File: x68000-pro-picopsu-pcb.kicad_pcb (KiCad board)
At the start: 2 copper layers, 209 x 98 mm, 27 parts, among them J1 Fan Header, J2 Screw_Terminal_01x07, J3 Screw_Terminal_01x07, J4 PicoPSU, U1 74LS04

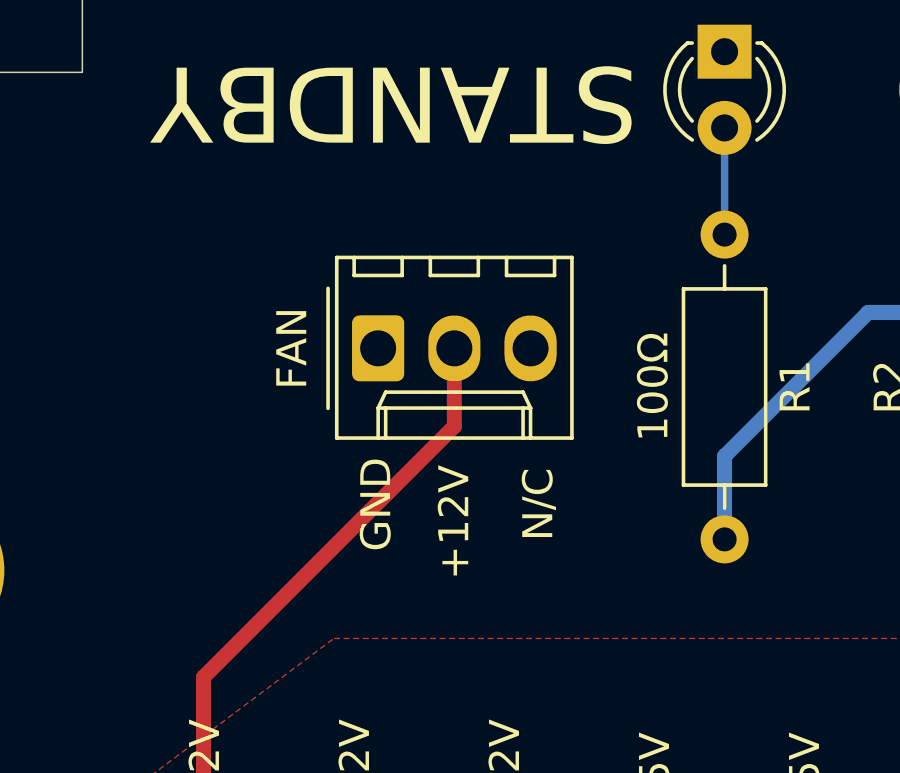
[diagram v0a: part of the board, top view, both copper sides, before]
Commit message: Move fan hed up a bit to make more room for wires
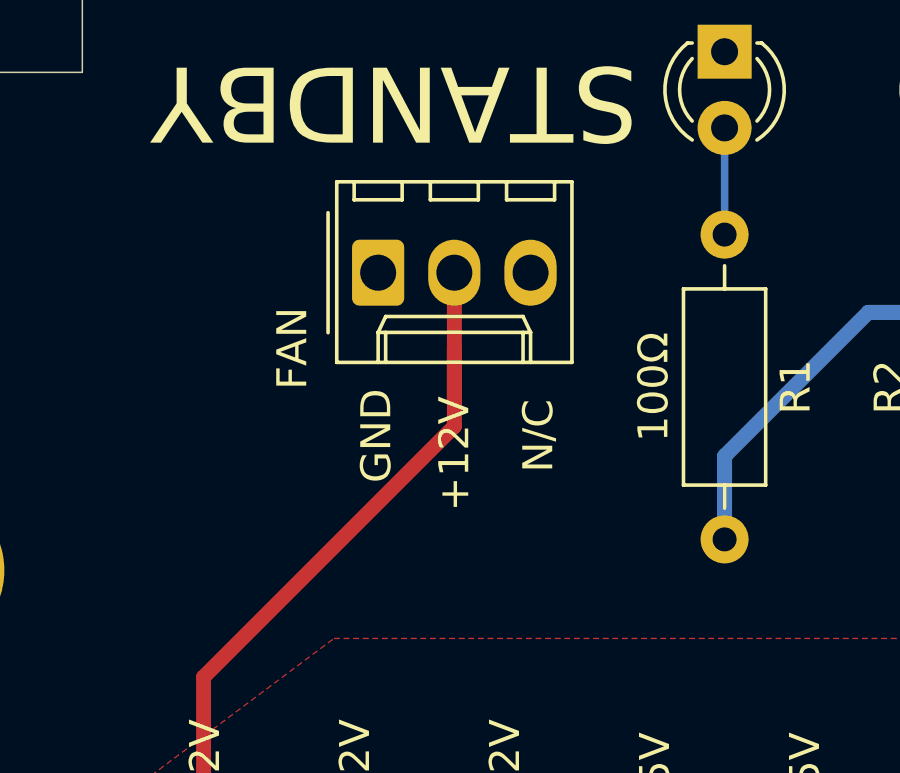
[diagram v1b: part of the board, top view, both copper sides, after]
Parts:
- moved J1 2.52 mm to (41.9, 90.7)
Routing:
- net /PSU_12V: track 24.8 -> 29.1 mm
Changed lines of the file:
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@@
     (thickness 1.6)
     (drawings 54)
-    (tracks 81)
+    (tracks 83)
     (zones 0)
     (modules 27)
@@
   )
   (setup
-    (last_trace_width 0.25)
+    (last_trace_width 0.5)
     (user_trace_width 0.5)
     (user_trace_width 2)
@@
   )
   (module Connector_Molex:Molex_KK-254_AE-6410-03A_1x03_P2.54mm_Vertical (layer F.Cu)
-    (at 41.86 93.2)
+    (at 41.86 90.678)
     (descr "Molex KK-254 Interconnect System, old/engineering part number: AE-6410-03A example for new part number: 22-27-2031, 3 Pins (http://www.molex.com/pdm_docs/sd/022272021_sd.pdf), generated with kicad-footprint-generator")
     (tags "connector Molex KK-254 side entry")
@@
     (effects (font (size 1 1) (thickness 0.15)))
   )
-  (gr_text N/C (at 47.2 98.4 90) (layer F.SilkS)
-    (effects (font (size 1 1) (thickness 0.15)))
-  )
-  (gr_text GND (at 41.8 98.4 90) (layer F.SilkS)
-    (effects (font (size 1 1) (thickness 0.15)))
-  )
-  (gr_text +12V (at 44.4 99 90) (layer F.SilkS)
+  (gr_text N/C (at 47.2 96.114 90) (layer F.SilkS)
+    (effects (font (size 1 1) (thickness 0.15)))
+  )
+  (gr_text GND (at 41.8 96.114 90) (layer F.SilkS)
+    (effects (font (size 1 1) (thickness 0.15)))
+  )
+  (gr_text +12V (at 44.4 96.714 90) (layer F.SilkS)
     (effects (font (size 1 1) (thickness 0.15)))
   )
@@
   (segment (start 84.12132 143) (end 85.12132 144) (width 0.25) (layer B.Cu) (net 15))
   (segment (start 36.04 114.554) (end 36.04 104.16) (width 0.5) (layer F.Cu) (net 16) (status 10))
-  (segment (start 44.4 95.8) (end 44.4 93.2) (width 0.5) (layer F.Cu) (net 16) (status 20))
   (segment (start 36.04 104.16) (end 44.4 95.8) (width 0.5) (layer F.Cu) (net 16))
+  (segment (start 44.4 94.946) (end 44.4 90.678) (width 0.5) (layer F.Cu) (net 16))
+  (segment (start 44.4 95.8) (end 44.4 94.946) (width 0.5) (layer F.Cu) (net 16))
+  (segment (start 44.4 94.946) (end 44.4 93.2) (width 0.5) (layer F.Cu) (net 16))
   (segment (start 108.637 74.855) (end 108.712 74.93) (width 0.25) (layer B.Cu) (net 17))
   (segment (start 108.637 71.302) (end 108.637 74.855) (width 0.25) (layer B.Cu) (net 17))

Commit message: Track cleanup
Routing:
- net /PSU_5V_STANDBY: track 173.4 -> 167.6 mm

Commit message: Update README
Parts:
- moved C1 22.5 mm to (142.1, 52.3)
- moved CONV_1 22.5 mm to (239.3, 117.1)
- moved G*** 22.5 mm to (218.2, 131.1)
- moved G*** 22.5 mm to (192.6, 48.5)
- moved G*** 22.5 mm to (244.2, 124.7)
- moved J4 22.5 mm to (108.8, 123.2)
- moved JP1 22.5 mm to (126.5, 61.9)
- moved JP2 22.5 mm to (131.6, 61.9)
- moved JP3 22.5 mm to (134.1, 45.7)
- moved JP5 22.5 mm to (124.0, 46.0)
- moved R1 22.5 mm to (71.2, 75.7)
- moved R3 22.5 mm to (111.9, 43.4)
- moved REF** 22.5 mm to (242.6, 43.4)
- moved TP3 22.5 mm to (99.8, 129.3)
- moved U1 22.5 mm to (121.3, 57.6)
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
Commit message: Routing fixes (thanks taqueso)
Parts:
- moved R3 22.4 mm to (113.8, 65.8), turned to 0 degrees
- moved TP2 5.36 mm to (97.5, 91.7)
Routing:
- net /~PS_ON: track 85.3 -> 64.0 mm
- net /POWER_ON_REQUEST: track 122.6 -> 112.5 mm
- net /PSU_5V_STANDBY: track 167.6 -> 159.1 mm
- net /PSU_12V: track 29.1 -> 24.6 mm
- net /PWR_OK: track 36.3 -> 39.9 mm
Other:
- board text added: "version 0.3, leadedsolder.com 2021"
- board text removed: "version 0.2, leadedsolder.com 2021"

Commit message: Mark for LED
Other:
- board text added: "+"
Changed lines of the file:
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@@
   (general
     (thickness 1.6)
-    (drawings 54)
+    (drawings 56)
     (tracks 70)
     (zones 0)
@@
   )
   (setup
-    (last_trace_width 2)
+    (last_trace_width 0.25)
     (user_trace_width 0.5)
     (user_trace_width 2)
@@
     )
   )
+  (gr_text + (at 73.025 72.898) (layer F.SilkS)
+    (effects (font (size 1 1) (thickness 0.15)))
+  )
+  (gr_text + (at 80.772 72.898) (layer F.SilkS)
+    (effects (font (size 1 1) (thickness 0.15)))
+  )
   (gr_text +12V (at 62.18 82.998 90) (layer F.SilkS)

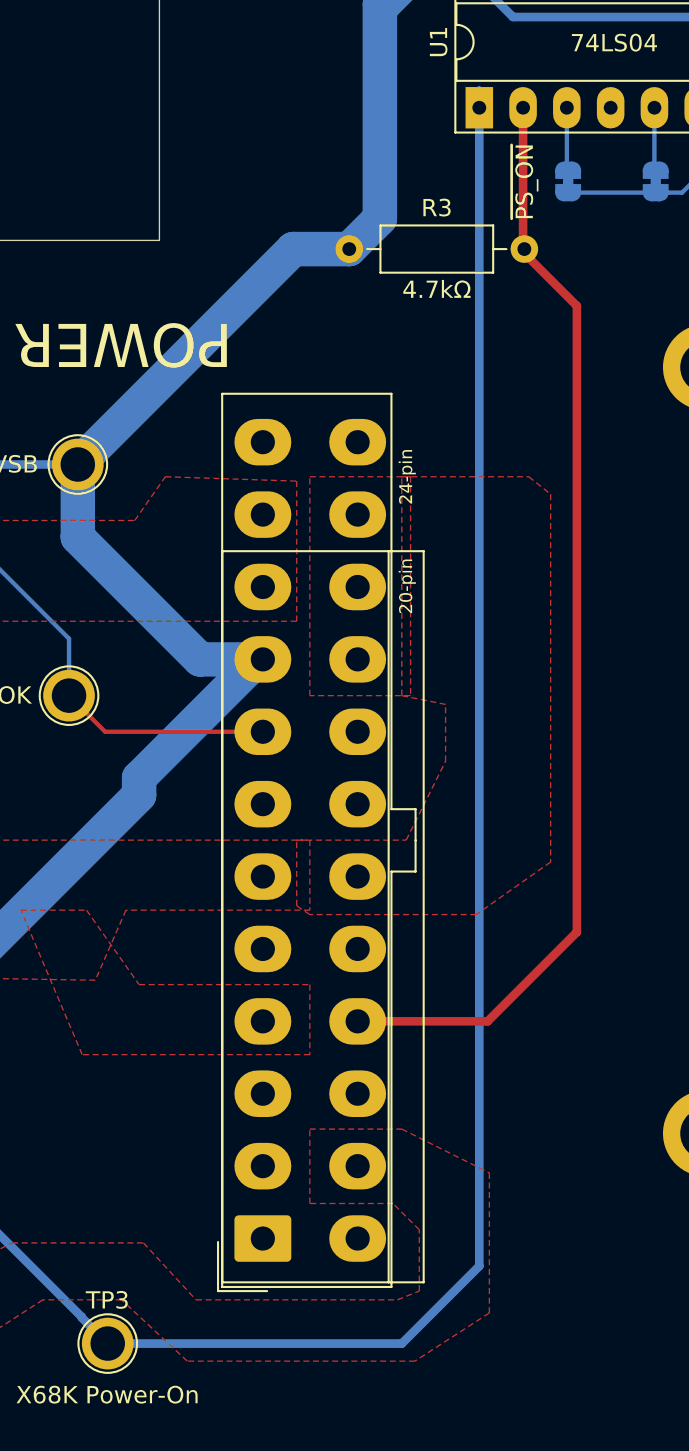
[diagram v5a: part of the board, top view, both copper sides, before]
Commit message: Fix screwup: move 4.7k pullup to input side of inverter
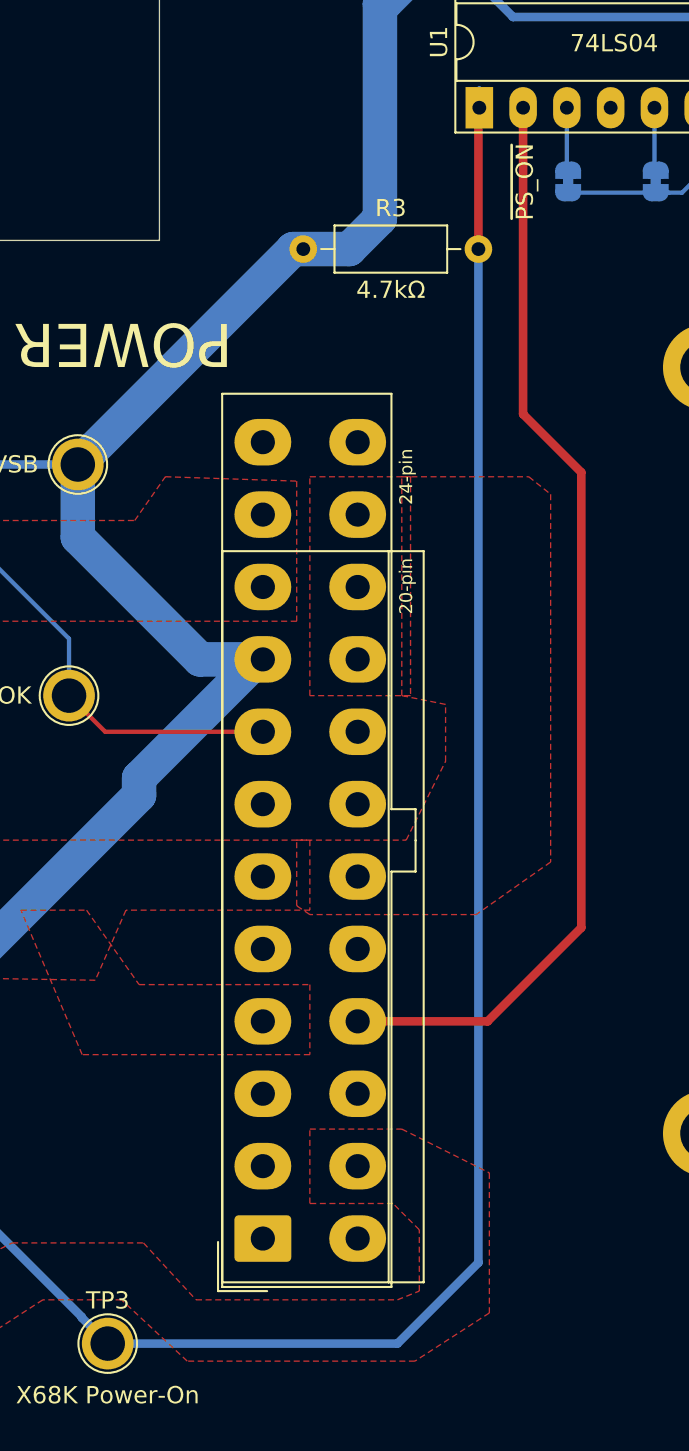
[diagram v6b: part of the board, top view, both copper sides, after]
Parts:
- moved R3 2.67 mm to (111.1, 65.8)
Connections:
- R3 pad 2: /~PS_ON -> /POWER_ON_REQUEST
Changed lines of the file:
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@@
     (thickness 1.6)
     (drawings 56)
-    (tracks 70)
+    (tracks 72)
     (zones 0)
     (modules 27)
@@
   )
   (setup
-    (last_trace_width 0.25)
+    (last_trace_width 0.5)
     (user_trace_width 0.5)
     (user_trace_width 2)
@@
   )
   (module Resistor_THT:R_Axial_DIN0207_L6.3mm_D2.5mm_P10.16mm_Horizontal (layer F.Cu)
-    (at 113.792 65.786)
+    (at 111.125 65.786)
     (descr "Resistor, Axial_DIN0207 series, Axial, Horizontal, pin pitch=10.16mm, 0.25W = 1/4W, length*diameter=6.3*2.5mm^2, http://cdn-reichelt.de/documents/datenblatt/B400/1_4W%23YAG.pdf")
     (tags "Resistor Axial_DIN0207 series Axial Horizontal pin pitch 10.16mm 0.25W = 1/4W length 6.3mm diameter 2.5mm")
@@
     (fp_line (start 1.93 -1.25) (end 1.93 1.25) (layer F.Fab) (width 0.1))
     (pad 2 thru_hole oval (at 10.16 0) (size 1.6 1.6) (drill 0.8) (layers *.Cu *.Mask)
-      (net 6 /~PS_ON))
+      (net 15 /POWER_ON_REQUEST))
     (pad 1 thru_hole circle (at 0 0) (size 1.6 1.6) (drill 0.8) (layers *.Cu *.Mask)
       (net 10 /PSU_5V_STANDBY))
@@
     )
   )
+  (gr_text ~PS_ON (at 123.98 61.884 90) (layer F.SilkS)
+    (effects (font (size 1 1) (thickness 0.15)))
+  )
   (gr_text + (at 73.025 72.898) (layer F.SilkS)
     (effects (font (size 1 1) (thickness 0.15)))
@@
   )
   (gr_text "version 0.3, leadedsolder.com 2021" (at 218.18 59.684) (layer F.SilkS)
-    (effects (font (size 1 1) (thickness 0.15)))
-  )
-  (gr_text ~PS_ON (at 123.98 61.884 90) (layer F.SilkS)
     (effects (font (size 1 1) (thickness 0.15)))
   )
@@
   (segment (start 131.572 62.514) (end 126.492 62.514) (width 0.25) (layer B.Cu) (net 2) (status 30))
   (segment (start 79.062 75.692) (end 79.062 72.136) (width 0.25) (layer B.Cu) (net 3) (status 30))
-  (segment (start 127 69.088) (end 123.877 65.965) (width 0.5) (layer F.Cu) (net 6) (status 20))
-  (segment (start 123.877 65.965) (end 123.877 57.586) (width 0.5) (layer F.Cu) (net 6) (status 30))
-  (segment (start 127 105.41) (end 127 69.088) (width 0.5) (layer F.Cu) (net 6))
-  (segment (start 114.28 110.59) (end 121.82 110.59) (width 0.5) (layer F.Cu) (net 6) (status 10))
-  (segment (start 121.82 110.59) (end 127 105.41) (width 0.5) (layer F.Cu) (net 6))
+  (segment (start 123.877 57.586) (end 123.877 75.363) (width 0.5) (layer F.Cu) (net 6))
+  (segment (start 123.877 75.363) (end 127.254 78.74) (width 0.5) (layer F.Cu) (net 6))
+  (segment (start 127.254 78.74) (end 127.254 105.156) (width 0.5) (layer F.Cu) (net 6))
+  (segment (start 121.82 110.59) (end 114.28 110.59) (width 0.5) (layer F.Cu) (net 6))
+  (segment (start 127.254 105.156) (end 121.82 110.59) (width 0.5) (layer F.Cu) (net 6))
   (segment (start 98.044 78.284) (end 75.98 78.284) (width 0.5) (layer B.Cu) (net 10) (status 10))
   (segment (start 71.188 83.076) (end 71.188 85.852) (width 0.5) (layer B.Cu) (net 10) (status 20))
@@
   (segment (start 89.408 80.264) (end 84.65 80.264) (width 0.25) (layer B.Cu) (net 11))
   (segment (start 121.337 56.441) (end 121.337 57.586) (width 0.25) (layer B.Cu) (net 15) (status 30))
-  (segment (start 121.337 57.586) (end 121.337 124.789) (width 0.5) (layer B.Cu) (net 15) (status 10))
-  (segment (start 116.842 129.284) (end 99.78 129.284) (width 0.5) (layer B.Cu) (net 15) (status 20))
-  (segment (start 121.337 124.789) (end 116.842 129.284) (width 0.5) (layer B.Cu) (net 15))
   (segment (start 98.280001 127.784001) (end 98.280001 127.744001) (width 0.5) (layer B.Cu) (net 15))
   (segment (start 99.78 129.284) (end 98.280001 127.784001) (width 0.5) (layer B.Cu) (net 15) (status 10))
   (segment (start 87.63 117.094) (end 84.102 117.094) (width 0.5) (layer B.Cu) (net 15) (status 20))
   (segment (start 98.280001 127.744001) (end 87.63 117.094) (width 0.5) (layer B.Cu) (net 15))
+  (segment (start 121.285 57.638) (end 121.337 57.586) (width 0.5) (layer F.Cu) (net 15))
+  (segment (start 121.285 65.786) (end 121.285 57.638) (width 0.5) (layer F.Cu) (net 15))
+  (segment (start 121.285 65.786) (end 121.285 124.587) (width 0.5) (layer B.Cu) (net 15))
+  (segment (start 116.588 129.284) (end 99.78 129.284) (width 0.5) (layer B.Cu) (net 15))
+  (segment (start 121.285 124.587) (end 116.588 129.284) (width 0.5) (layer B.Cu) (net 15))
   (segment (start 62.18 99.198) (end 63.82 100.838) (width 2) (layer F.Cu) (net 16) (status 20))
   (segment (start 62.18 76.962) (end 62.18 99.198) (width 2) (layer F.Cu) (net 16) (status 10))

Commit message: V0.3 + assembly instructions
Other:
- board text added: "version 0.3, leadedsolder.com 2021–2022"
- board text removed: "version 0.3, leadedsolder.com 2021"
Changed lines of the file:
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@@
   )
   (setup
-    (last_trace_width 0.5)
+    (last_trace_width 0.25)
     (user_trace_width 0.5)
     (user_trace_width 2)
@@
       (drillshape 0)
       (scaleselection 1)
-      (outputdirectory "plot"))
+      (outputdirectory "x68000-pro-picopsu-v0.3"))
   )
   (net 0 "")
@@
     (effects (font (size 2.5 2.5) (thickness 0.15)))
   )
-  (gr_text "version 0.3, leadedsolder.com 2021" (at 218.18 59.684) (layer F.SilkS)
-    (effects (font (size 1 1) (thickness 0.15)))
+  (gr_text "version 0.3, leadedsolder.com 2021–2022" (at 208.25 60) (layer F.SilkS)
+    (effects (font (size 1.5 1.5) (thickness 0.15)))
   )
   (gr_text N/C (at 64.98 82.398 90) (layer F.SilkS)
